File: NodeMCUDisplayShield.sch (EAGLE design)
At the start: 2 parts

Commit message: Single-sided version
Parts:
- added X1: 332-02, con-garry:332-02
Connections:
- net LED renamed D3
- net SCK renamed D5_SCK
- net SDI/MOSI renamed D7_SDI/MOSI
- net SODI/MISO renamed D6_SODI/MISO
- removed net CS: ESP8266.1, TFT+TOUCH.12
- removed net D/C: ESP8266.2, TFT+TOUCH.10
- removed net T_CS: ESP8266.4, TFT+TOUCH.4
- removed net T_IRQ: ESP8266.10, TFT+TOUCH.1
- new net D1: ESP8266.1, TFT+TOUCH.1
- new net D2: ESP8266.2, TFT+TOUCH.4
- new net D4: ESP8266.4, TFT+TOUCH.10
- new net D8: ESP8266.10, TFT+TOUCH.12
- net GND: now also X1-2.S
- net VCC: now also X1-1.S
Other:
- note added: "CS"
- note added: "D/C"
- note added: "LED"
- note added: "T_CS"
- note added: "T_IRQ"
- note removed: "3V3"
- note removed: "D1"
- note removed: "D2"
- note removed: "D3"
- note removed: "D4"
- note removed: "D5"
- note removed: "D6"
- note removed: "D7"
- note removed: "D8"
- note removed: "GND"
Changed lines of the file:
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@@
 <?xml version="1.0" encoding="utf-8"?>
 <!DOCTYPE eagle SYSTEM "eagle.dtd">
-<eagle version="8.1.0">
+<eagle version="8.3.1">
 <drawing>
 <settings>
 <setting alwaysvectorfont="no"/>
+<setting keepoldvectorfont="yes"/>
 <setting verticaltext="up"/>
 </settings>
@@
 <part name="TFT+TOUCH" library="pinhead" deviceset="PINHD-1X14" device=""/>
 <part name="ESP8266" library="pinhead" deviceset="PINHD-1X10" device=""/>
+<part name="X1" library="con-garry" library_urn="urn:adsk.eagle:library:147" deviceset="332-02" device="" package3d_urn="urn:adsk.eagle:package:6810/1"/>
 </parts>
 <sheets>
 <sheet>
 <plain>
-<text x="22.86" y="68.58" size="1.778" layer="95">D1</text>
-<text x="22.86" y="66.04" size="1.778" layer="95">D2</text>
-<text x="22.86" y="63.5" size="1.778" layer="95">D3</text>
-<text x="22.86" y="60.96" size="1.778" layer="95">D4</text>
-<text x="20.32" y="58.42" size="1.778" layer="95">3V3</text>
-<text x="20.32" y="55.88" size="1.778" layer="95">GND</text>
-<text x="22.86" y="53.34" size="1.778" layer="95">D5</text>
-<text x="22.86" y="50.8" size="1.778" layer="95">D6</text>
-<text x="22.86" y="48.26" size="1.778" layer="95">D7</text>
-<text x="22.86" y="45.72" size="1.778" layer="95">D8</text>
 <text x="58.42" y="58.42" size="1.778" layer="95">T_CLK</text>
 <text x="58.42" y="66.04" size="1.778" layer="95">T_DO</text>
 <text x="58.42" y="63.5" size="1.778" layer="95">T_DIN</text>
-<text x="60.96" y="50.8" size="1.778" layer="95">SCK</text>
+<text x="58.42" y="50.8" size="1.778" layer="95">SCK</text>
 <text x="55.88" y="48.26" size="1.778" layer="95">SDI/MOSI</text>
 <text x="58.42" y="43.18" size="1.778" layer="95">RESET</text>
 <text x="53.34" y="55.88" size="1.778" layer="95">SODI/MISO</text>
+<text x="58.42" y="68.58" size="1.778" layer="95">T_IRQ</text>
+<text x="58.42" y="60.96" size="1.778" layer="95">T_CS</text>
+<text x="58.42" y="53.34" size="1.778" layer="95">LED</text>
+<text x="58.42" y="45.72" size="1.778" layer="95">D/C</text>
+<text x="58.42" y="40.64" size="1.778" layer="95">CS</text>
 </plain>
 <instances>
 <instance part="TFT+TOUCH" gate="A" x="73.66" y="53.34"/>
 <instance part="ESP8266" gate="A" x="33.02" y="58.42"/>
+<instance part="X1" gate="-1" x="20.32" y="38.1"/>
+<instance part="X1" gate="-2" x="20.32" y="35.56"/>
 </instances>
 <busses>
 </busses>
 <nets>
-<net name="T_IRQ" class="0">
-<segment>
-<pinref part="TFT+TOUCH" gate="A" pin="1"/>
-<wire x1="71.12" y1="68.58" x2="38.1" y2="68.58" width="0.1524" layer="91"/>
-<label x="38.1" y="68.58" size="1.778" layer="95"/>
-</segment>
+<net name="D8" class="0">
 <segment>
 <pinref part="ESP8266" gate="A" pin="10"/>
@@
 <label x="10.16" y="45.72" size="1.778" layer="95"/>
 </segment>
-</net>
-<net name="T_CS" class="0">
-<segment>
-<pinref part="TFT+TOUCH" gate="A" pin="4"/>
-<wire x1="71.12" y1="60.96" x2="38.1" y2="60.96" width="0.1524" layer="91"/>
-<label x="38.1" y="60.96" size="1.778" layer="95"/>
-</segment>
+<segment>
+<pinref part="TFT+TOUCH" gate="A" pin="12"/>
+<wire x1="71.12" y1="40.64" x2="38.1" y2="40.64" width="0.1524" layer="91"/>
+<label x="38.1" y="40.64" size="1.778" layer="95"/>
+</segment>
+</net>
+<net name="D4" class="0">
 <segment>
 <pinref part="ESP8266" gate="A" pin="4"/>
@@
 <label x="10.16" y="60.96" size="1.778" layer="95"/>
 </segment>
-</net>
-<net name="SODI/MISO" class="0">
+<segment>
+<pinref part="TFT+TOUCH" gate="A" pin="10"/>
+<wire x1="71.12" y1="45.72" x2="38.1" y2="45.72" width="0.1524" layer="91"/>
+<label x="38.1" y="45.72" size="1.778" layer="95"/>
+</segment>
+</net>
+<net name="D6_SODI/MISO" class="0">
 <segment>
 <pinref part="TFT+TOUCH" gate="A" pin="6"/>
@@
 </segment>
 </net>
-<net name="LED" class="1">
+<net name="D3" class="1">
 <segment>
 <pinref part="TFT+TOUCH" gate="A" pin="7"/>
@@
 </segment>
 </net>
-<net name="SCK" class="0">
+<net name="D5_SCK" class="0">
 <segment>
 <pinref part="TFT+TOUCH" gate="A" pin="8"/>
@@
 </segment>
 </net>
-<net name="SDI/MOSI" class="0">
+<net name="D7_SDI/MOSI" class="0">
 <segment>
 <pinref part="TFT+TOUCH" gate="A" pin="9"/>
@@
 </segment>
 </net>
-<net name="D/C" class="0">
-<segment>
-<pinref part="TFT+TOUCH" gate="A" pin="10"/>
-<wire x1="71.12" y1="45.72" x2="38.1" y2="45.72" width="0.1524" layer="91"/>
-<label x="38.1" y="45.72" size="1.778" layer="95"/>
-</segment>
+<net name="D2" class="0">
 <segment>
 <pinref part="ESP8266" gate="A" pin="2"/>
@@
 <label x="10.16" y="66.04" size="1.778" layer="95"/>
 </segment>
-</net>
-<net name="CS" class="0">
-<segment>
-<pinref part="TFT+TOUCH" gate="A" pin="12"/>
-<wire x1="71.12" y1="40.64" x2="38.1" y2="40.64" width="0.1524" layer="91"/>
-<label x="38.1" y="40.64" size="1.778" layer="95"/>
-</segment>
+<segment>
+<pinref part="TFT+TOUCH" gate="A" pin="4"/>
+<wire x1="71.12" y1="60.96" x2="38.1" y2="60.96" width="0.1524" layer="91"/>
+<label x="38.1" y="60.96" size="1.778" layer="95"/>
+</segment>
+</net>
+<net name="D1" class="0">
 <segment>
 <pinref part="ESP8266" gate="A" pin="1"/>
@@
 <label x="10.16" y="68.58" size="1.778" layer="95"/>
 </segment>
+<segment>
+<pinref part="TFT+TOUCH" gate="A" pin="1"/>
+<wire x1="71.12" y1="68.58" x2="38.1" y2="68.58" width="0.1524" layer="91"/>
+<label x="38.1" y="68.58" size="1.778" layer="95"/>
+</segment>
 </net>
 <net name="GND" class="1">
@@
 <label x="10.16" y="55.88" size="1.778" layer="95"/>
 </segment>
+<segment>
+<pinref part="X1" gate="-2" pin="S"/>
+<wire x1="17.78" y1="35.56" x2="10.16" y2="35.56" width="0.1524" layer="91"/>
+<label x="10.16" y="35.56" size="1.778" layer="95"/>
+</segment>
 </net>
 <net name="VCC" class="1">
@@
 <wire x1="71.12" y1="43.18" x2="38.1" y2="43.18" width="0.1524" layer="91"/>
 <label x="38.1" y="43.18" size="1.778" layer="95"/>
+</segment>
+<segment>
+<pinref part="X1" gate="-1" pin="S"/>
+<wire x1="17.78" y1="38.1" x2="10.16" y2="38.1" width="0.1524" layer="91"/>
+<label x="10.16" y="38.1" size="1.778" layer="95"/>
 </segment>
 </net>
@@
 </schematic>
 </drawing>
+<compatibility>
+<note version="8.2" severity="warning">
+Since Version 8.2, EAGLE supports online libraries. The ids
+of those online libraries will not be understood (or retained)
+with this version.
+</note>
+<note version="8.3" severity="warning">
+Since Version 8.3, EAGLE supports URNs for individual library
+assets (packages, symbols, and devices). The URNs of those assets
+will not be understood (or retained) with this version.
+</note>
+<note version="8.3" severity="warning">
+Since Version 8.3, EAGLE supports the association of 3D packages
+with devices in libraries, schematics, and board files. Those 3D
+packages will not be understood (or retained) with this version.
+</note>
+</compatibility>
 </eagle>

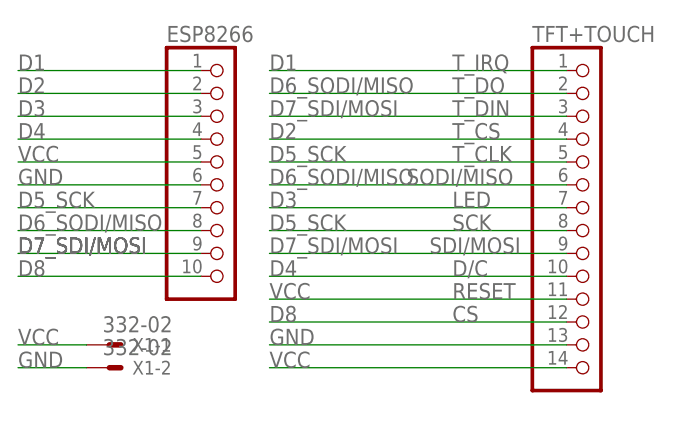
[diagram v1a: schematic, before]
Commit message: https://pcbs.io/share/zd3qw SIngle-sided.
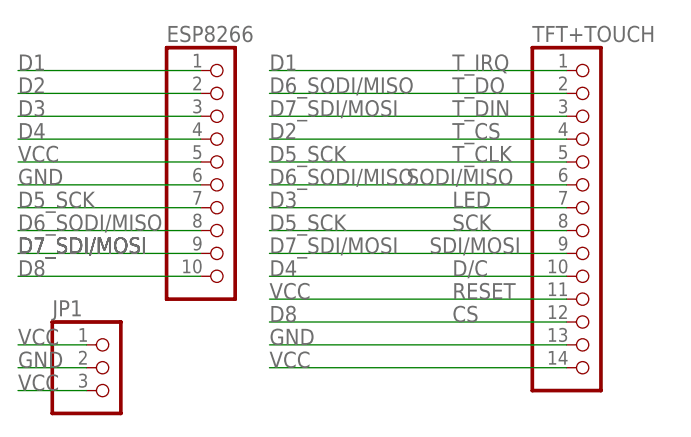
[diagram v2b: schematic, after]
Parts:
- removed X1: 332-02, con-garry:332-02
- added JP1: (no value), pinhead_v2:PINHD-1X3/OCT
- ESP8266: device pinhead:PINHD-1X10 -> pinhead_v2:PINHD-1X10/OCT
- TFT+TOUCH: device pinhead:PINHD-1X14 -> pinhead_v2:PINHD-1X14/OCT
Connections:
- net GND: now also JP1.2; no longer X1-2.S
- net VCC: now also JP1.1, JP1.3; no longer X1-1.S
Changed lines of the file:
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@@
 </classes>
 <parts>
-<part name="TFT+TOUCH" library="pinhead" deviceset="PINHD-1X14" device=""/>
-<part name="ESP8266" library="pinhead" deviceset="PINHD-1X10" device=""/>
-<part name="X1" library="con-garry" library_urn="urn:adsk.eagle:library:147" deviceset="332-02" device="" package3d_urn="urn:adsk.eagle:package:6810/1"/>
+<part name="TFT+TOUCH" library="pinhead_v2" deviceset="PINHD-1X14" device="/OCT"/>
+<part name="ESP8266" library="pinhead_v2" deviceset="PINHD-1X10" device="/OCT"/>
+<part name="JP1" library="pinhead_v2" deviceset="PINHD-1X3" device="/OCT"/>
 </parts>
 <sheets>
@@
 <instance part="TFT+TOUCH" gate="A" x="73.66" y="53.34"/>
 <instance part="ESP8266" gate="A" x="33.02" y="58.42"/>
-<instance part="X1" gate="-1" x="20.32" y="38.1"/>
-<instance part="X1" gate="-2" x="20.32" y="35.56"/>
+<instance part="JP1" gate="A" x="20.32" y="35.56"/>
 </instances>
 <busses>
@@
 </segment>
 <segment>
-<pinref part="X1" gate="-2" pin="S"/>
 <wire x1="17.78" y1="35.56" x2="10.16" y2="35.56" width="0.1524" layer="91"/>
 <label x="10.16" y="35.56" size="1.778" layer="95"/>
+<pinref part="JP1" gate="A" pin="2"/>
 </segment>
 </net>
@@
 </segment>
 <segment>
-<pinref part="X1" gate="-1" pin="S"/>
 <wire x1="17.78" y1="38.1" x2="10.16" y2="38.1" width="0.1524" layer="91"/>
 <label x="10.16" y="38.1" size="1.778" layer="95"/>
+<pinref part="JP1" gate="A" pin="1"/>
+</segment>
+<segment>
+<pinref part="JP1" gate="A" pin="3"/>
+<wire x1="17.78" y1="33.02" x2="10.16" y2="33.02" width="0.1524" layer="91"/>
+<label x="10.16" y="33.02" size="1.778" layer="95"/>
 </segment>
 </net>
@@
 </schematic>
 </drawing>
-<compatibility>
-<note version="8.2" severity="warning">
-Since Version 8.2, EAGLE supports online libraries. The ids
-of those online libraries will not be understood (or retained)
-with this version.
-</note>
-<note version="8.3" severity="warning">
-Since Version 8.3, EAGLE supports URNs for individual library
-assets (packages, symbols, and devices). The URNs of those assets
-will not be understood (or retained) with this version.
-</note>
-<note version="8.3" severity="warning">
-Since Version 8.3, EAGLE supports the association of 3D packages
-with devices in libraries, schematics, and board files. Those 3D
-packages will not be understood (or retained) with this version.
-</note>
-</compatibility>
 </eagle>

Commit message: pdf updated, short info in schema added
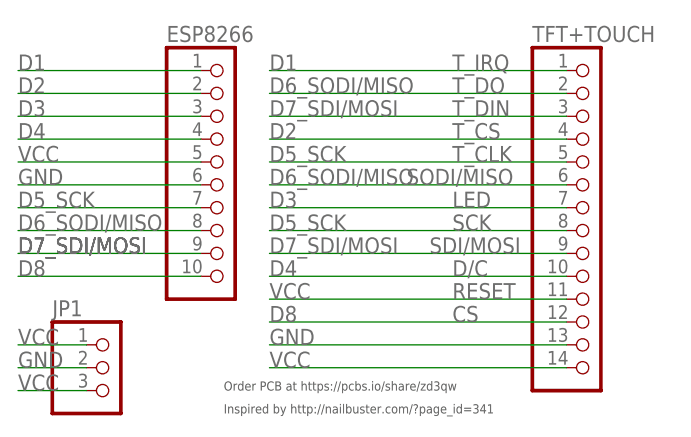
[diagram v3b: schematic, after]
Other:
- note added: "Inspired by http://nailbuster.com/?page_id=341"
- note added: "Order PCB at https://pcbs.io/share/zd3qw"
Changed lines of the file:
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@@
 <text x="58.42" y="45.72" size="1.778" layer="95">D/C</text>
 <text x="58.42" y="40.64" size="1.778" layer="95">CS</text>
+<text x="33.02" y="30.48" size="1.016" layer="97">Inspired by http://nailbuster.com/?page_id=341</text>
+<text x="33.02" y="33.02" size="1.016" layer="97">Order PCB at https://pcbs.io/share/zd3qw</text>
 </plain>
 <instances>
